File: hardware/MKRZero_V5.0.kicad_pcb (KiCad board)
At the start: 2 copper layers, 80 x 60 mm, 55 parts, among them IC1 PCF8523T, J1 USB_B_Micro, J2 2X3_SMD_MALE, J3 AMPHENOL_114-00841-68, J6 Conn_01x08_Pin, J7 Conn_01x04_Pin, J8 PJ-320A, Q1 32.768KHz, SW1 RotaryEncoder_Switch_MP, SW2 RotaryEncoder_Switch_MP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

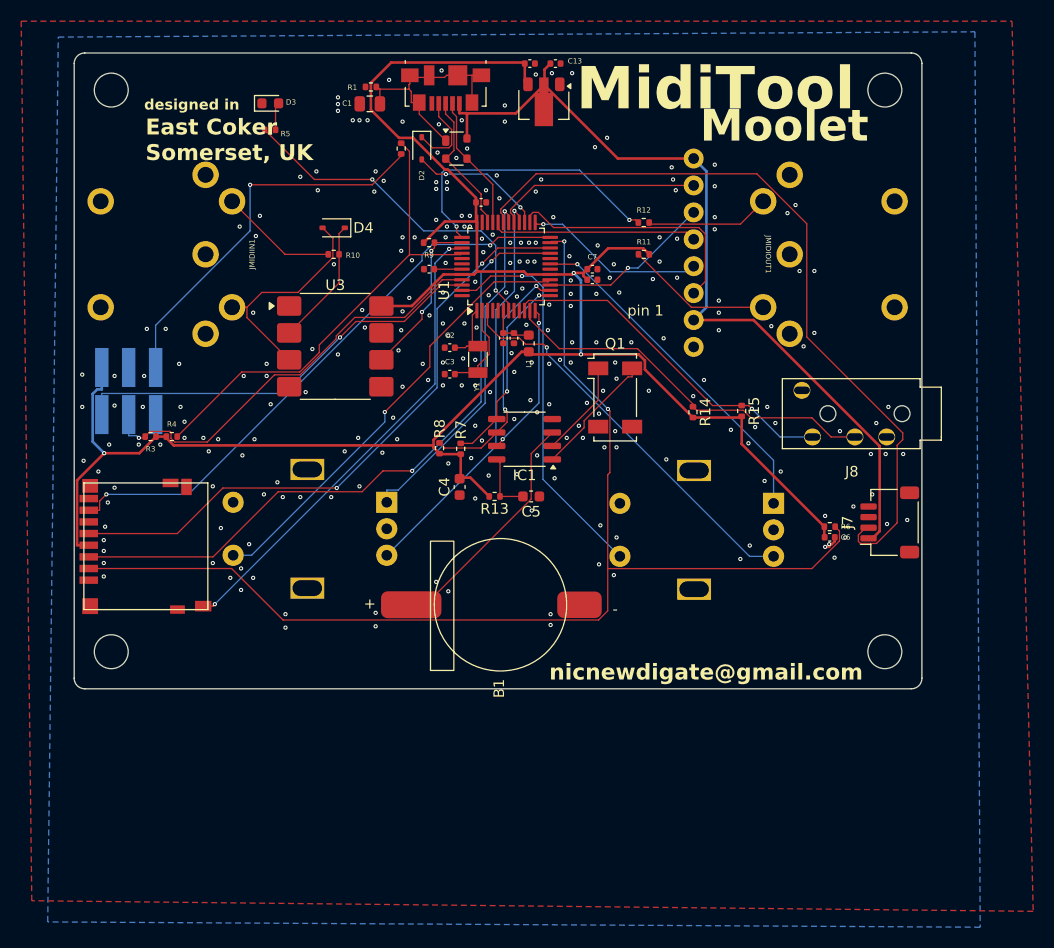
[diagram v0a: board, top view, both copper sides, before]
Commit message: correction to battery holder footprint
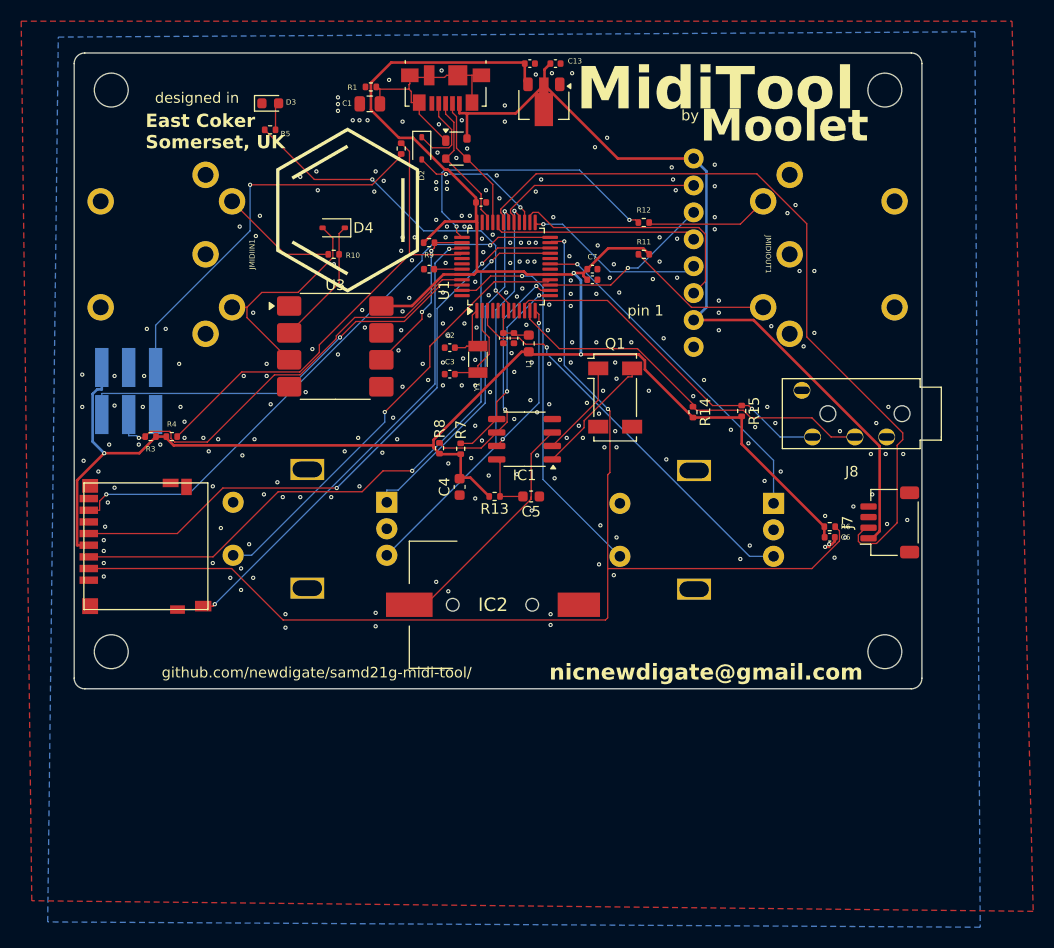
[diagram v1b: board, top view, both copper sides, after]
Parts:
- removed B1: CR1220, MKRZero_V5.0:CR1220-2 Q&J
- added IC2: CR1220-2, CR12202:CR12202, F.Cu at (39.6, 52.1)
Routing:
- net Net-(IC1-VBAT): track 22.6 -> 24.3 mm
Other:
- board text added: "by"
- board text added: "github.com/newdigate/samd21g-midi-tool/"

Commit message: add second pair of mounting holes for DIN5 midi connector socket to make compatible with different DIN5 variations
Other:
- board text added: "github.com/newdigate/ samd21g-midi-tool/"
- board text removed: "github.com/newdigate/samd21g-midi-tool/"
